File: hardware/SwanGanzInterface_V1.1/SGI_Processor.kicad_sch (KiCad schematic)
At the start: 34 parts, among them J14 Conn_01x03_Pin, J2 Conn_01x09_Pin, SW2 NRST, SW3 UP, SW4 ENTER, SW5 DOWN, SW6 LEFT, SW7 RIGHT, U4 XM0G3507QPMRQ1, Y1 ABM8AIG-40.000MHZ-12-2Z-T3

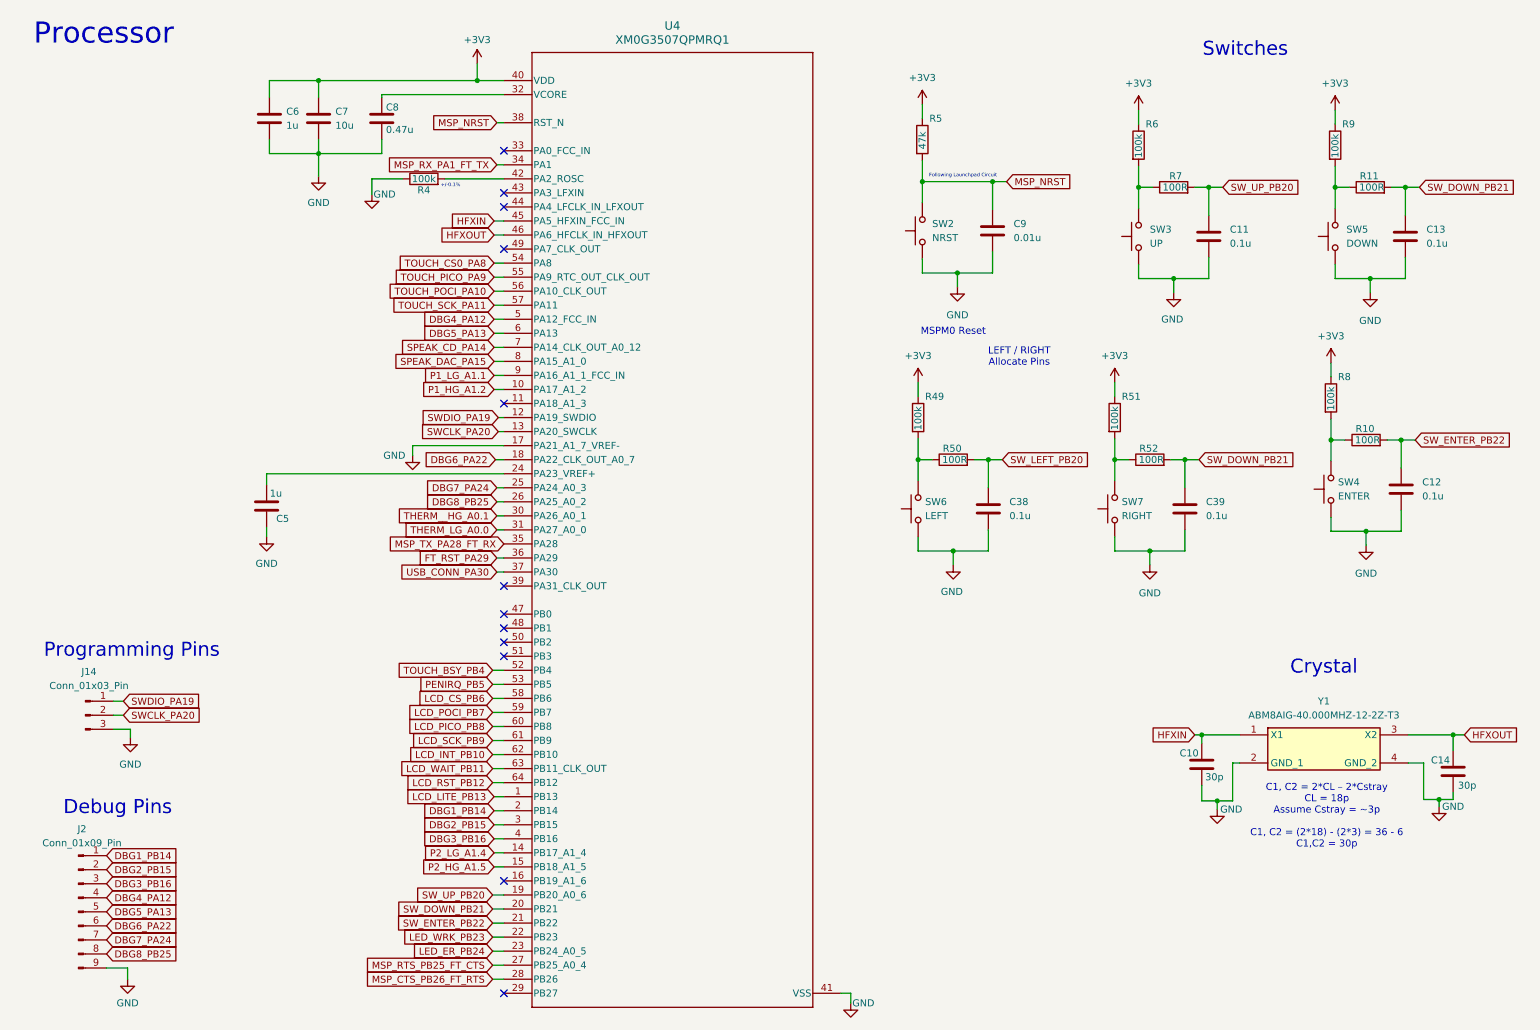
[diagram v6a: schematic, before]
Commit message: Button pin allocation, layout of power and ft, general layout
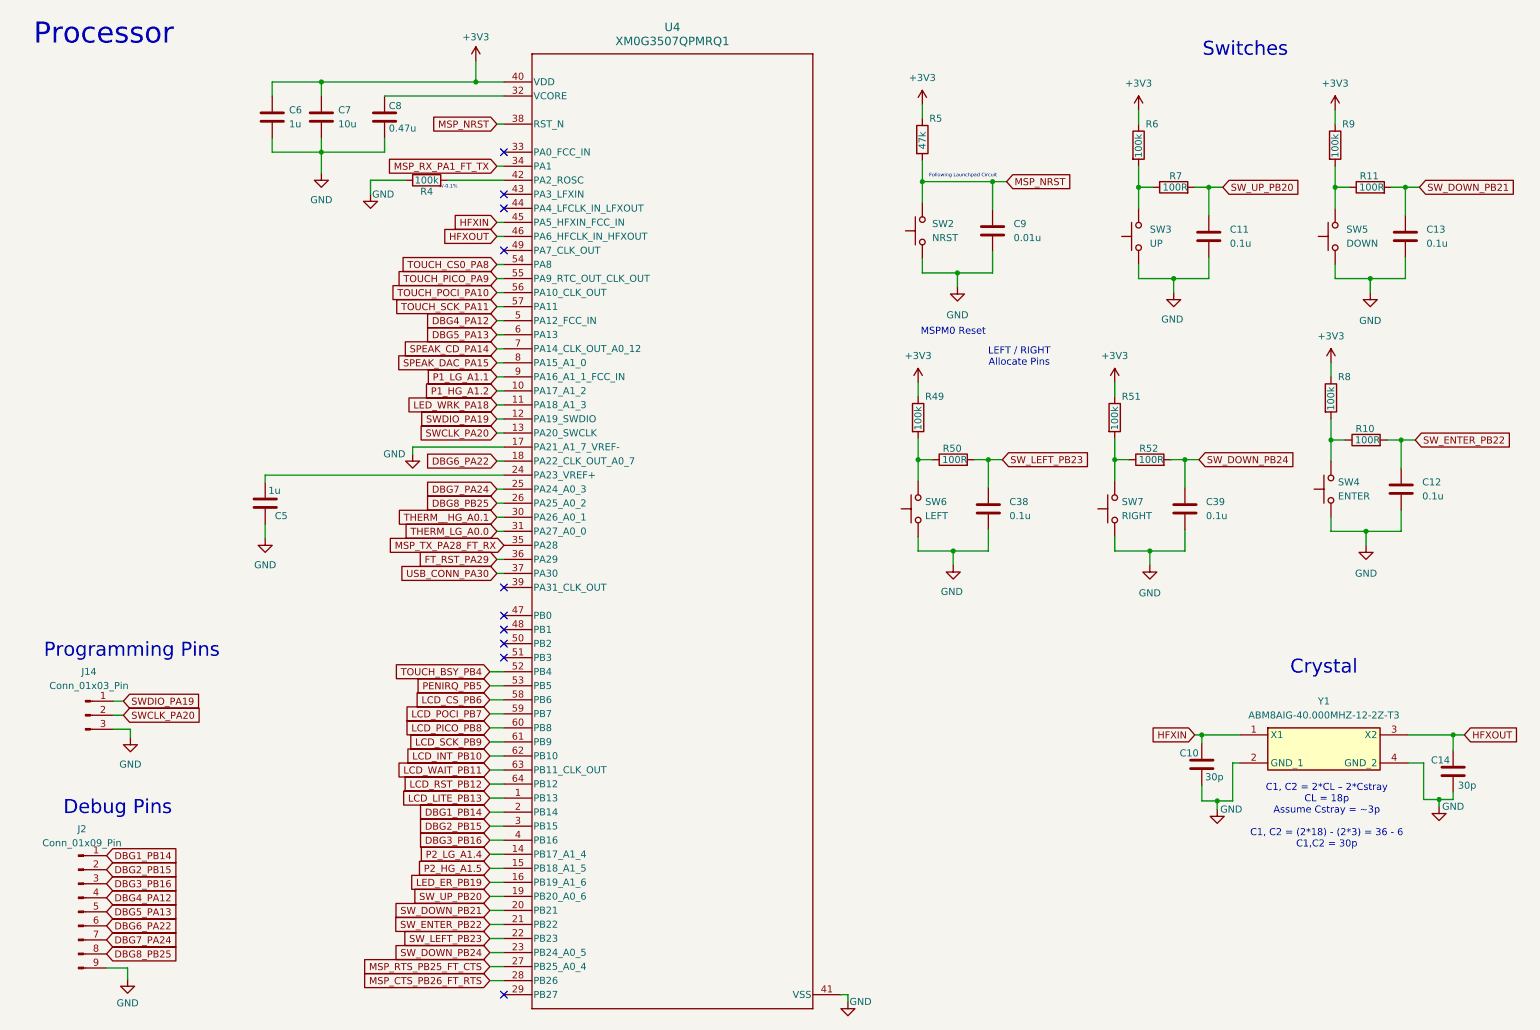
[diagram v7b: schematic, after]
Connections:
- net SW_LEFT_PB20 is gone; now on net SW_LEFT_PB23: C38.1, R50.2
- net SW_DOWN_PB21: no longer C39.1, R52.2
- net LED_WRK_PA18: now reaches U4.11 (PA18_A1_3)
- net LED_ER_PB19: now reaches U4.16 (PB19_A1_6)
- net LED_ER_PB24 renamed SW_DOWN_PB24
- net SW_DOWN_PB24: now also C39.1, R52.2
- net LED_WRK_PB23 renamed SW_LEFT_PB23
- no-connect marks 12 -> 10
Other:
- moved on the sheet: C5, C6, C7, C8, R4

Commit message: Digital Traces
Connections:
- net USB_CONN_PA7: now reaches U4.49 (PA7_CLK_OUT)
- net USB_CONN_PA30: no longer names the net of U4.37 (PA30)
- no-connect marks 10 -> 9
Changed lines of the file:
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@@
 	(text "+/-0.1%"
 		(exclude_from_sim no)
-		(at 90.17 44.45 0)
+		(at 91.44 44.45 0)
 		(effects
 			(font
@@
 	)
 	(no_connect
-		(at 100.33 55.88)
-	)
-	(no_connect
 		(at 100.33 45.72)
 	)
@@
 	(wire
 		(pts
+			(xy 99.06 55.88) (xy 100.33 55.88)
+		)
+		(stroke
+			(width 0)
+			(type default)
+		)
+	)
+	(wire
+		(pts
 			(xy 97.79 175.26) (xy 100.33 175.26)
 		)
@@
 	(wire
 		(pts
+			(xy 99.06 109.22) (xy 100.33 109.22)
+		)
+		(stroke
+			(width 0)
+			(type default)
+		)
+	)
+	(wire
+		(pts
 			(xy 187.96 93.726) (xy 190.5 93.726)
 		)
@@
 		)
 	)
+	(global_label "P1_LG_A1.1"
+		(shape input)
+		(at 99.06 78.74 180)
+		(fields_autoplaced yes)
+		(effects
+			(font
+				(size 1.27 1.27)
+			)
+			(justify right)
+		)
+		(property "Intersheetrefs" "${INTERSHEET_REFS}"
+			(at 85.2496 78.74 0)
+			(effects
+				(font
+					(size 1.27 1.27)
+				)
+				(justify right)
+				(hide yes)
+			)
+		)
+	)
+	(global_label "DBG2_PB15"
+		(shape input)
+		(at 97.79 160.02 180)
+		(fields_autoplaced yes)
+		(effects
+			(font
+				(size 1.27 1.27)
+			)
+			(justify right)
+		)
+		(property "Intersheetrefs" "${INTERSHEET_REFS}"
+			(at 83.8587 160.02 0)
+			(effects
+				(font
+					(size 1.27 1.27)
+				)
+				(justify right)
+				(hide yes)
+			)
+		)
+	)
+	(global_label "HFXOUT"
+		(shape input)
+		(at 99.06 53.34 180)
+		(fields_autoplaced yes)
+		(effects
+			(font
+				(size 1.27 1.27)
+			)
+			(justify right)
+		)
+		(property "Intersheetrefs" "${INTERSHEET_REFS}"
+			(at 88.8176 53.34 0)
+			(effects
+				(font
+					(size 1.27 1.27)
+				)
+				(justify right)
+				(hide yes)
+			)
+		)
+	)
+	(global_label "P2_LG_A1.4"
+		(shape input)
+		(at 97.79 165.1 180)
+		(fields_autoplaced yes)
+		(effects
+			(font
+				(size 1.27 1.27)
+			)
+			(justify right)
+		)
+		(property "Intersheetrefs" "${INTERSHEET_REFS}"
+			(at 83.9796 165.1 0)
+			(effects
+				(font
+					(size 1.27 1.27)
+				)
+				(justify right)
+				(hide yes)
+			)
+		)
+	)
 	(global_label "MSP_TX_PA28_FT_RX"
 		(shape input)
-		(at 100.33 109.22 180)
-		(fields_autoplaced yes)
-		(effects
-			(font
-				(size 1.27 1.27)
-			)
-			(justify right)
-		)
-		(property "Intersheetrefs" "${INTERSHEET_REFS}"
-			(at 78.0531 109.22 0)
-			(effects
-				(font
-					(size 1.27 1.27)
-				)
-				(justify right)
-				(hide yes)
-			)
-		)
-	)
-	(global_label "P1_LG_A1.1"
-		(shape input)
-		(at 99.06 78.74 180)
-		(fields_autoplaced yes)
-		(effects
-			(font
-				(size 1.27 1.27)
-			)
-			(justify right)
-		)
-		(property "Intersheetrefs" "${INTERSHEET_REFS}"
-			(at 85.2496 78.74 0)
-			(effects
-				(font
-					(size 1.27 1.27)
-				)
-				(justify right)
-				(hide yes)
-			)
-		)
-	)
-	(global_label "DBG2_PB15"
-		(shape input)
-		(at 97.79 160.02 180)
-		(fields_autoplaced yes)
-		(effects
-			(font
-				(size 1.27 1.27)
-			)
-			(justify right)
-		)
-		(property "Intersheetrefs" "${INTERSHEET_REFS}"
-			(at 83.8587 160.02 0)
-			(effects
-				(font
-					(size 1.27 1.27)
-				)
-				(justify right)
-				(hide yes)
-			)
-		)
-	)
-	(global_label "HFXOUT"
-		(shape input)
-		(at 99.06 53.34 180)
-		(fields_autoplaced yes)
-		(effects
-			(font
-				(size 1.27 1.27)
-			)
-			(justify right)
-		)
-		(property "Intersheetrefs" "${INTERSHEET_REFS}"
-			(at 88.8176 53.34 0)
-			(effects
-				(font
-					(size 1.27 1.27)
-				)
-				(justify right)
-				(hide yes)
-			)
-		)
-	)
-	(global_label "P2_LG_A1.4"
-		(shape input)
-		(at 97.79 165.1 180)
-		(fields_autoplaced yes)
-		(effects
-			(font
-				(size 1.27 1.27)
-			)
-			(justify right)
-		)
-		(property "Intersheetrefs" "${INTERSHEET_REFS}"
-			(at 83.9796 165.1 0)
+		(at 99.06 109.22 180)
+		(fields_autoplaced yes)
+		(effects
+			(font
+				(size 1.27 1.27)
+			)
+			(justify right)
+		)
+		(property "Intersheetrefs" "${INTERSHEET_REFS}"
+			(at 76.7831 109.22 0)
 			(effects
 				(font
@@
 		)
 	)
+	(global_label "MSP_RX_PA1_FT_TX"
+		(shape input)
+		(at 99.06 40.64 180)
+		(fields_autoplaced yes)
+		(effects
+			(font
+				(size 1.27 1.27)
+			)
+			(justify right)
+		)
+		(property "Intersheetrefs" "${INTERSHEET_REFS}"
+			(at 77.9926 40.64 0)
+			(effects
+				(font
+					(size 1.27 1.27)
+				)
+				(justify right)
+				(hide yes)
+			)
+		)
+	)
 	(global_label "DBG7_PA24"
 		(shape input)
@@
 		)
 	)
+	(global_label "USB_CONN_PA7"
+		(shape input)
+		(at 99.06 55.88 180)
+		(fields_autoplaced yes)
+		(effects
+			(font
+				(size 1.27 1.27)
+			)
+			(justify right)
+		)
+		(property "Intersheetrefs" "${INTERSHEET_REFS}"
+			(at 81.5 55.88 0)
+			(effects
+				(font
+					(size 1.27 1.27)
+				)
+				(justify right)
+				(hide yes)
+			)
+		)
+	)
 	(global_label "MSP_NRST"
 		(shape input)
@@
 		)
 	)
-	(global_label "USB_CONN_PA30"
-		(shape input)
-		(at 99.06 114.3 180)
-		(fields_autoplaced yes)
-		(effects
-			(font
-				(size 1.27 1.27)
-			)
-			(justify right)
-		)
-		(property "Intersheetrefs" "${INTERSHEET_REFS}"
-			(at 80.2905 114.3 0)
-			(effects
-				(font
-					(size 1.27 1.27)
-				)
-				(justify right)
-				(hide yes)
-			)
-		)
-	)
 	(global_label "HFXIN"
 		(shape input)
@@
 			(effects
 				(font
-					(size 1.27 1.27)
-				)
-				(justify right)
-				(hide yes)
-			)
-		)
-	)
-	(global_label "MSP_RX_PA1_FT_TX"
-		(shape input)
-		(at 99.06 40.64 180)
-		(fields_autoplaced yes)
-		(effects
-			(font
-				(size 1.27 1.27)
-			)
-			(justify right)
-		)
-		(property "Intersheetrefs" "${INTERSHEET_REFS}"
-			(at 77.9926 40.64 0)
-			(effects
-				(font
